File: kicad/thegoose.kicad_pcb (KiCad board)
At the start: 4 copper layers, 88.5 x 47 mm, 175 parts, among them J1 USB_C_Receptacle_USB2.0_16P, J11 Balance, J12 LED stick, J3 XT30UPB-M, J4 USB-A host, J5 IO 3x6 RA, Q1 AO4407A, Q2 80N03F, Q3 80N03F, SW1 Power, SW2 BOOT, U1 DRV8848, U10 RP2354A, U11 SRV05-4, U12 SY6280AAC, U13 BQ7791501, U14 74AHCT1G125, U2 DRV8848, U3 DRV8848, U4 AP64500SP-13, U5 CH224A, U6 SRV05-4, U7 BQ25798, U8 HT7550-1, U9 XC6206P332MR, Y1 12MHz

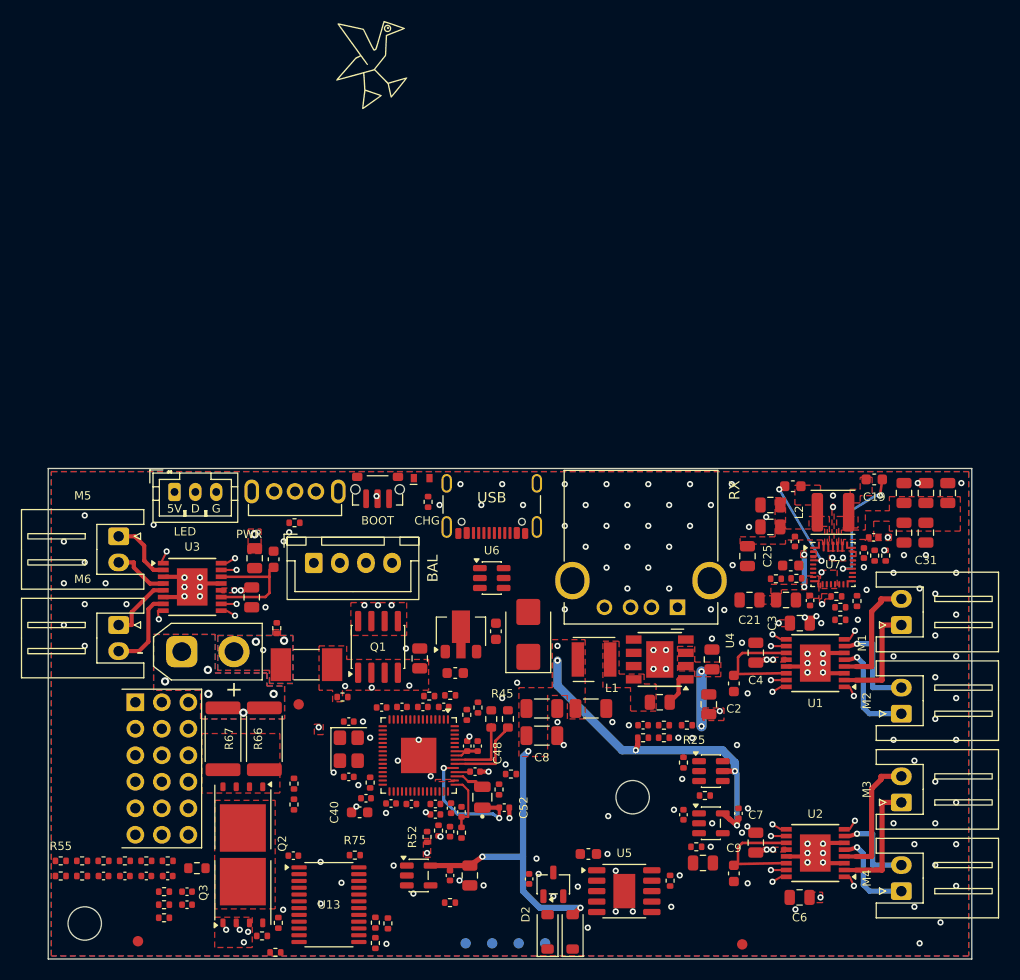
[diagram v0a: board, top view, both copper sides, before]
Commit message: Route rev 2 on a 6-layer board
Four layers couldn't route the fan-out around the RP2354A, so the board
moves to JLC's standard 1.6 mm 6-layer stack (JLC06161H-3313, ENIG,
via-in-pad): F signals, In1 GND, In2 signals, In3 power planes, In4 GND,
B signals. Placement is unchanged.

Review 53 passes every gate: nothing unrouted, 0 DRC errors. The critic
stopped at 3.9 after 10 iterations; the open findings are in
build/review/pcb/LOG.md, including DVDD pin 23's 100 nF (C54) sitting
about 11 mm of copper away.

Also adds the inner3/inner4 review views, the 6-layer quotes in
PARTS.md, and fixes the core-regulator note's cap names.

Co-Authored-By: Claude Opus 5.5 <noreply@anthropic.com>
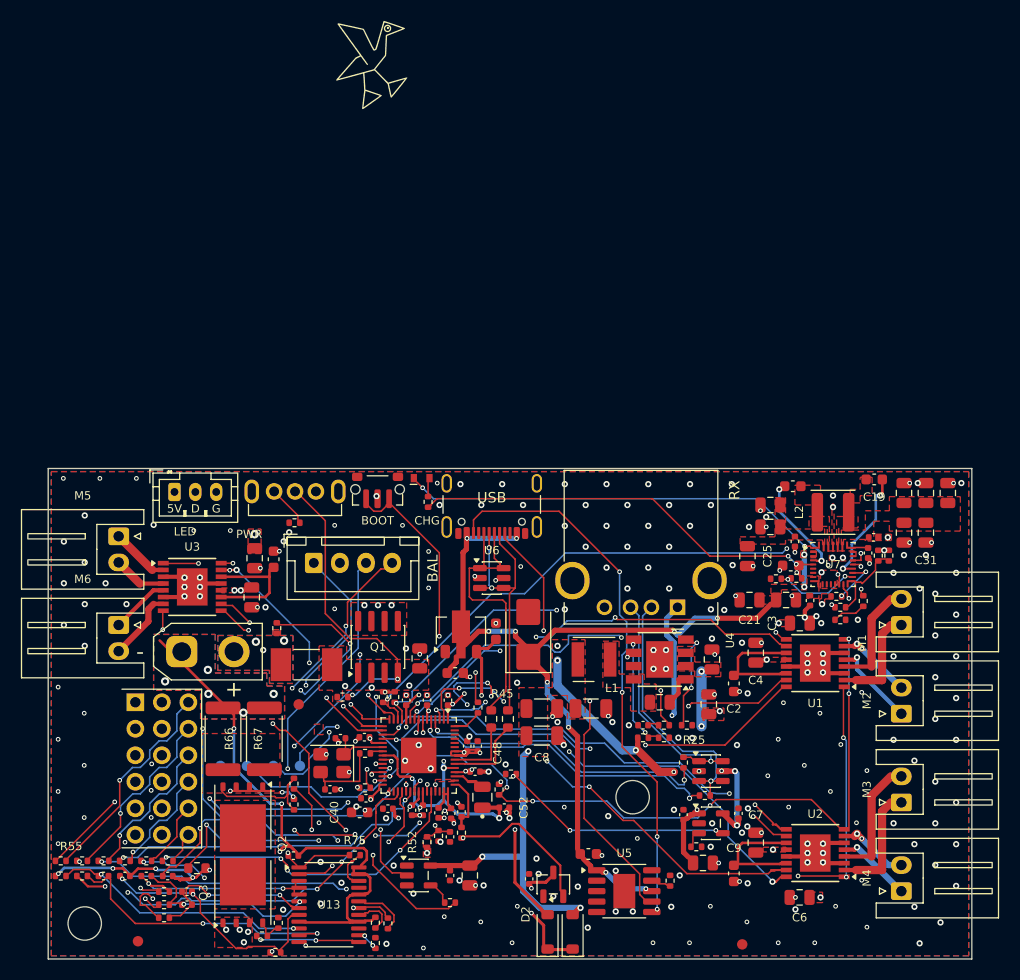
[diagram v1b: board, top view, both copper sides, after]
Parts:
- moved TP4 35.5 mm to (116.5, 128.5)
- moved TP3 31.1 mm to (119.0, 128.5)
- moved TP2 27.0 mm to (121.6, 128.5)
- moved TP1 23.3 mm to (124.1, 128.5)
- moved R37 12.0 mm to (130.3, 130.6), turned to 0 degrees
- moved R39 6.42 mm to (132.1, 121.9), turned to -90 degrees
- moved R38 3.31 mm to (133.2, 121.9), turned to -90 degrees
- moved C43 3.29 mm to (130.3, 125.8)
- moved R43 2.84 mm to (130.4, 127.3), turned to 180 degrees
- moved C45 2.33 mm to (134.8, 132.8), turned to -90 degrees
- moved C57 2.16 mm to (127.0, 130.8)
- moved Y1 2.09 mm to (127.2, 128.2), turned to 180 degrees
- moved C56 1.79 mm to (128.0, 125.8), turned to 180 degrees
- moved C55 1.25 mm to (135.9, 132.8), turned to -90 degrees
- moved C41 0.76 mm to (138.3, 122.2), turned to 90 degrees
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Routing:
- net DRV_FAULT: track 2.75 -> 107.6 mm, vias 3 -> 8
- net DRV_SLEEP: track 3.16 -> 105.2 mm, vias 3 -> 5
- net VBUS: track 3.10 -> 77.7 mm, vias 2 -> 12
- net /Power & charging/BAT_N: track 0.00 -> 73.7 mm, vias 5 -> 13
- net +3V3: track 2.26 -> 71.1 mm, vias 0 -> 18
- net I2C_SCL: track 0.00 -> 67.0 mm, vias 0 -> 4
- net CHG_INT: track 0.00 -> 56.4 mm, vias 0 -> 3
- net GPIO4_M1A: track 0.93 -> 53.9 mm, vias 1 -> 5
- net Net-(J12-Pin_2): track 0.00 -> 52.7 mm, vias 0 -> 3
- net I2C_SDA: track 0.00 -> 52.5 mm, vias 0 -> 3
- net Net-(J1-CC2): track 0.00 -> 52.2 mm, vias 0 -> 4
- net /Power & charging/CELL1: track 0.00 -> 44.7 mm, vias 0 -> 3
- net /Power & charging/REGN: track 0.00 -> 44.4 mm, vias 0 -> 4
- net GPIO0_M3A: track 0.93 -> 44.2 mm, vias 1 -> 4
- net /Power & charging/CELL2: track 0.00 -> 43.1 mm, vias 0 -> 2
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- added copper zone on In3.Cu, net +3V3
- added copper zone on In3.Cu, net GND
- added copper zone on In4.Cu, net GND
- added copper zone on In3.Cu, net VBAT
- added copper zone on In3.Cu, net VCC
- added copper zone on In3.Cu, net VSYS
- removed copper zone on In2.Cu, net VBAT
- removed copper zone on In2.Cu, net VCC
- removed copper zone on In2.Cu, net VSYS
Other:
- copper layers 4 -> 6
- board text added: "SWD / RUN / GND pads TP1-TP4 (bottom): SWCLK, SWDIO, RUN, GND at 2.54 mm, TP1 nearest U10 (east end)"
- board text removed: "SWD / RUN / GND pads TP1-TP4 (bottom): SWCLK, SWDIO, RUN, GND at 2.54 mm"

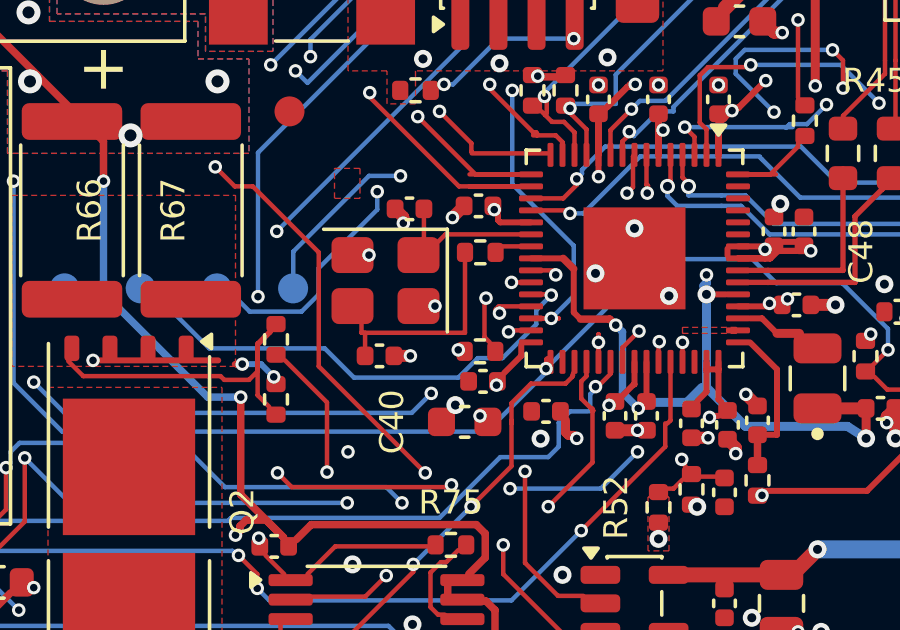
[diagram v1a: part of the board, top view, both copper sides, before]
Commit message: Move C54 next to DVDD pin 23
C54 (pin 23's 100 nF) sat at U10's bottom-left corner, 11 mm of copper
from the pin through two vias and an In2 jumper. It now sits directly
left of pin 23 in R43's old spot: about 1.3 mm of F.Cu, with a GND via
in its pad.

To make room, R43 turns vertical under Y1, and XOUT runs down between
Y1 and C54. SWDIO passes under C54 to a new via and goes straight west
on B.Cu to TP2, which drops the In2 detour. Y1 pad 4's GND via moves
into the pad, and the IO1 via shifts 0.5 mm left.

Review 54: all gates pass, no new DRC types.

Co-Authored-By: Claude Opus 5.5 <noreply@anthropic.com>
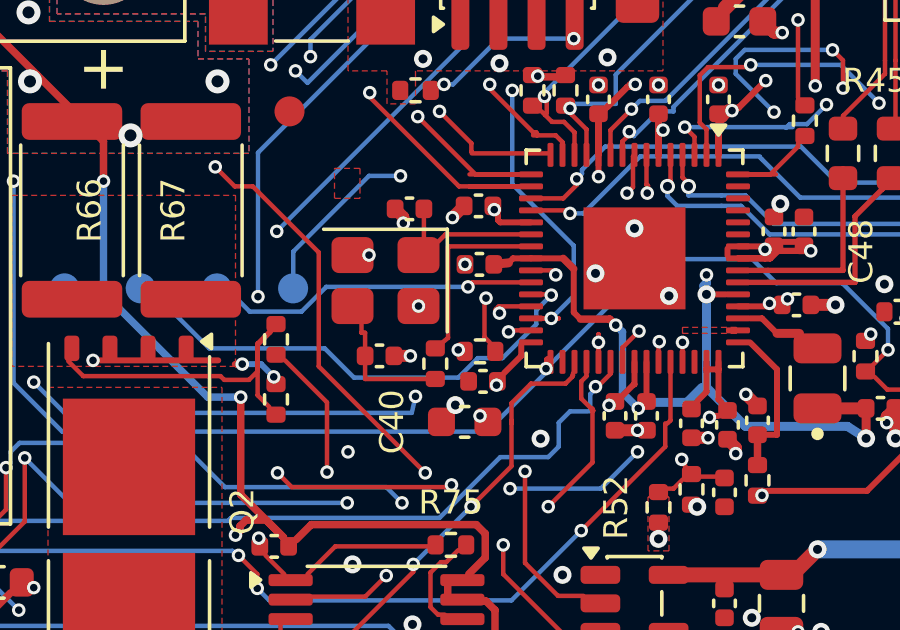
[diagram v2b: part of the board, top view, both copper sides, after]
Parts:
- moved C54 5.38 mm to (130.3, 127.7)
- moved R43 4.00 mm to (128.9, 131.0), turned to -90 degrees
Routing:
- net Net-(U10-SWDIO): track 16.9 -> 10.7 mm, vias 2 -> 1
- net Net-(U10-XOUT): track 1.18 -> 6.37 mm
- net Net-(C57-Pad1): track 7.38 -> 4.48 mm
- net +1V1: track 36.1 -> 34.1 mm, vias 7 -> 6
- net GND: track 42.9 -> 42.4 mm, vias 256 -> 257

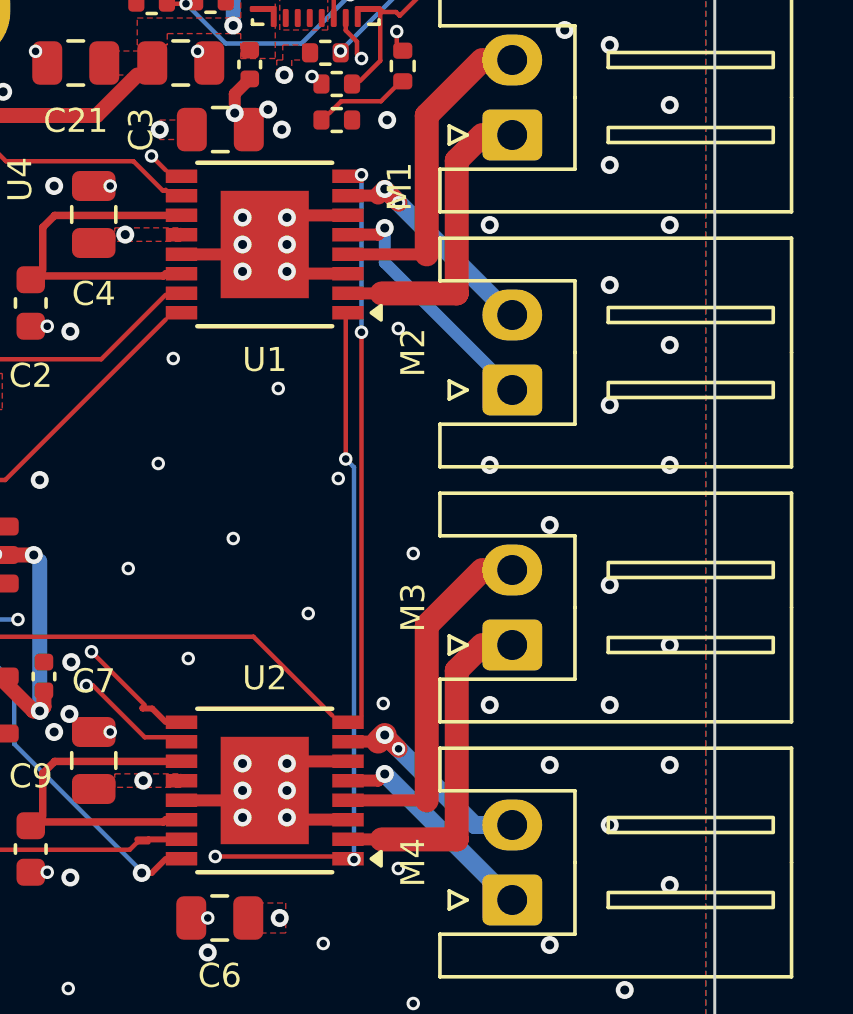
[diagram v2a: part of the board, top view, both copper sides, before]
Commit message: Double the M2/M4 output vias and record the pre-order checks
M2 and M4's OUT1 each changed layers through a single 0.3 mm via. Each
now has a second via beside the first, tied on both layers. OUT2's B.Cu
run leaves from its own second via to make room, and M2 OUT1's B.Cu run
is widened to 0.6 mm. Every motor output that changes layers now does it
through two vias.

PARTS.md records two datasheet checks:
- CH224A: CFG1 = 6.8 kOhm requests 9 V (WCH datasheet Table 5-1), and the
  VHV/VBUS hookup matches the reference schematic.
- SRV05-4: the R+O pinout matches the symbol (I/O on 1, 3, 4 and 6, VP on
  5, GND on 2).

Review 55: all gates pass, no new DRC types.

Co-Authored-By: Claude Opus 5.5 <noreply@anthropic.com>
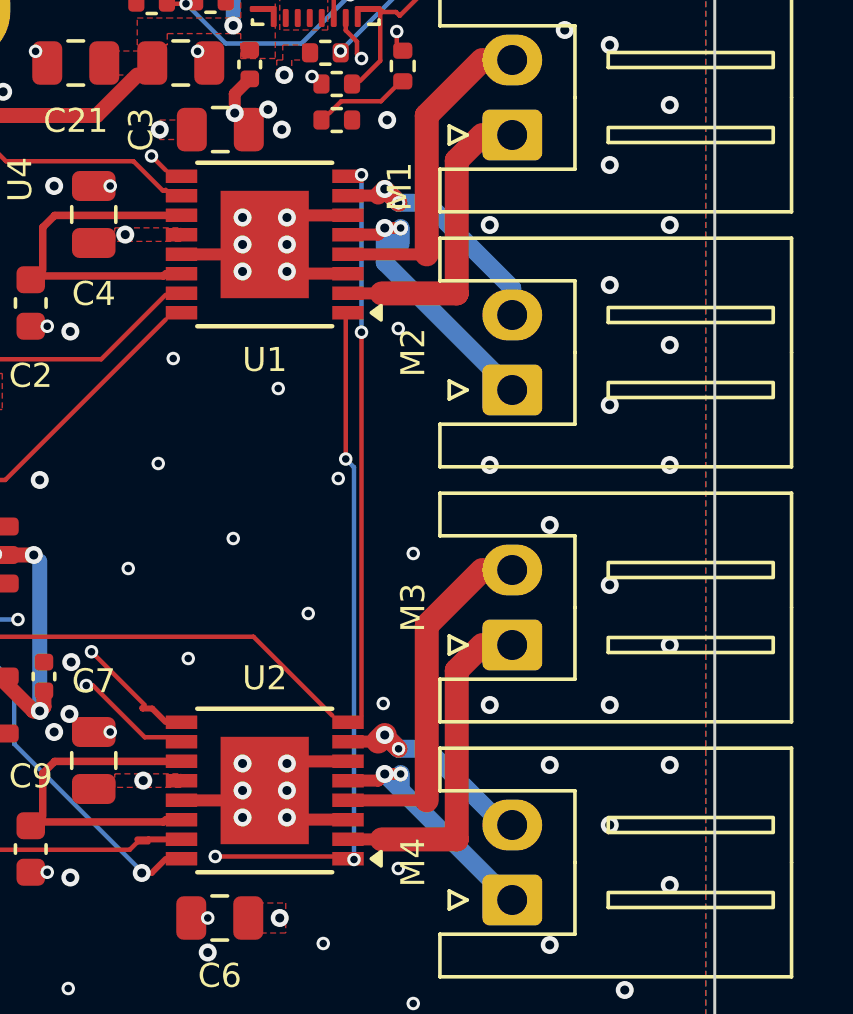
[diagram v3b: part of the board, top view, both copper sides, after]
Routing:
- net Net-(M4-OUT1): track 6.78 -> 7.84 mm, vias 1 -> 2
- net Net-(M2-OUT1): track 7.95 -> 9.01 mm, vias 1 -> 2
- net Net-(M2-OUT2): track 7.43 -> 7.95 mm
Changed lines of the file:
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@@
 	)
 	(segment
+		(start 177.5 118.1)
+		(end 178.03 118.1)
+		(width 0.4)
+		(layer "F.Cu")
+		(net "Net-(M2-OUT1)")
+	)
+	(segment
 		(start 177.28 118.32)
 		(end 177.5 118.1)
@@
 	)
 	(via
+		(at 178.03 118.1)
+		(size 0.5)
+		(drill 0.25)
+		(layers "F.Cu" "B.Cu")
+		(net "Net-(M2-OUT1)")
+	)
+	(via
 		(at 177.5 118.1)
 		(size 0.6)
@@
 	)
 	(segment
+		(start 178.03 118.1)
+		(end 178.03 118.63)
+		(width 0.6)
+		(layer "B.Cu")
+		(net "Net-(M2-OUT1)")
+	)
+	(segment
 		(start 177.5 119.25)
 		(end 181.75 123.5)
-		(width 0.4)
+		(width 0.6)
 		(locked yes)
 		(layer "B.Cu")
@@
 		(start 177.5 118.1)
 		(end 177.5 119.25)
-		(width 0.4)
+		(width 0.6)
 		(locked yes)
 		(layer "B.Cu")
@@
 	)
 	(segment
-		(start 181.7 121)
+		(start 177.5 116.8)
+		(end 177.96 117.26)
+		(width 0.6)
+		(layer "B.Cu")
+		(net "Net-(M2-OUT2)")
+	)
+	(segment
+		(start 181.75 120.11)
 		(end 181.75 121)
-		(width 0.8)
-		(locked yes)
+		(width 0.6)
 		(layer "B.Cu")
 		(net "Net-(M2-OUT2)")
 	)
 	(segment
-		(start 177.5 116.8)
-		(end 181.7 121)
+		(start 178.9 117.26)
+		(end 181.75 120.11)
+		(width 0.6)
+		(layer "B.Cu")
+		(net "Net-(M2-OUT2)")
+	)
+	(segment
+		(start 177.96 117.26)
+		(end 178.9 117.26)
 		(width 0.6)
-		(locked yes)
 		(layer "B.Cu")
 		(net "Net-(M2-OUT2)")
@@
 	)
 	(segment
+		(start 177.5 136.3)
+		(end 178.03 136.3)
+		(width 0.4)
+		(layer "F.Cu")
+		(net "Net-(M4-OUT1)")
+	)
+	(segment
 		(start 177.28 136.52)
 		(end 177.5 136.3)
@@
 	)
 	(via
+		(at 178.03 136.3)
+		(size 0.5)
+		(drill 0.25)
+		(layers "F.Cu" "B.Cu")
+		(net "Net-(M4-OUT1)")
+	)
+	(via
 		(at 177.5 136.3)
 		(size 0.6)
@@
 	)
 	(segment
+		(start 178.03 136.3)
+		(end 178.03 136.83)
+		(width 0.6)
+		(layer "B.Cu")
+		(net "Net-(M4-OUT1)")
+	)
+	(segment
 		(start 177.5 136.3)
 		(end 181.7 140.5)
@@
 	)
 	(segment
-		(start 180.5 138)
+		(start 181.44 138)
 		(end 181.75 138)
 		(width 0.6)
-		(locked yes)
 		(layer "B.Cu")
 		(net "Net-(M4-OUT2)")
@@
 	(segment
 		(start 177.5 135)
-		(end 180.5 138)
+		(end 177.96 135.46)
+		(width 0.6)
+		(layer "B.Cu")
+		(net "Net-(M4-OUT2)")
+	)
+	(segment
+		(start 177.96 135.46)
+		(end 178.9 135.46)
+		(width 0.6)
+		(layer "B.Cu")
+		(net "Net-(M4-OUT2)")
+	)
+	(segment
+		(start 178.9 135.46)
+		(end 181.44 138)
 		(width 0.6)
-		(locked yes)
 		(layer "B.Cu")
 		(net "Net-(M4-OUT2)")
